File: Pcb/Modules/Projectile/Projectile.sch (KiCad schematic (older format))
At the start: 34 parts, among them J1 JACK_RJ45, Q1 Q_NMOS_GSD, U1 OPA320, U2 OPA320, X1 HOLE, X2 HOLE, X3 HOLE, X4 HOLE

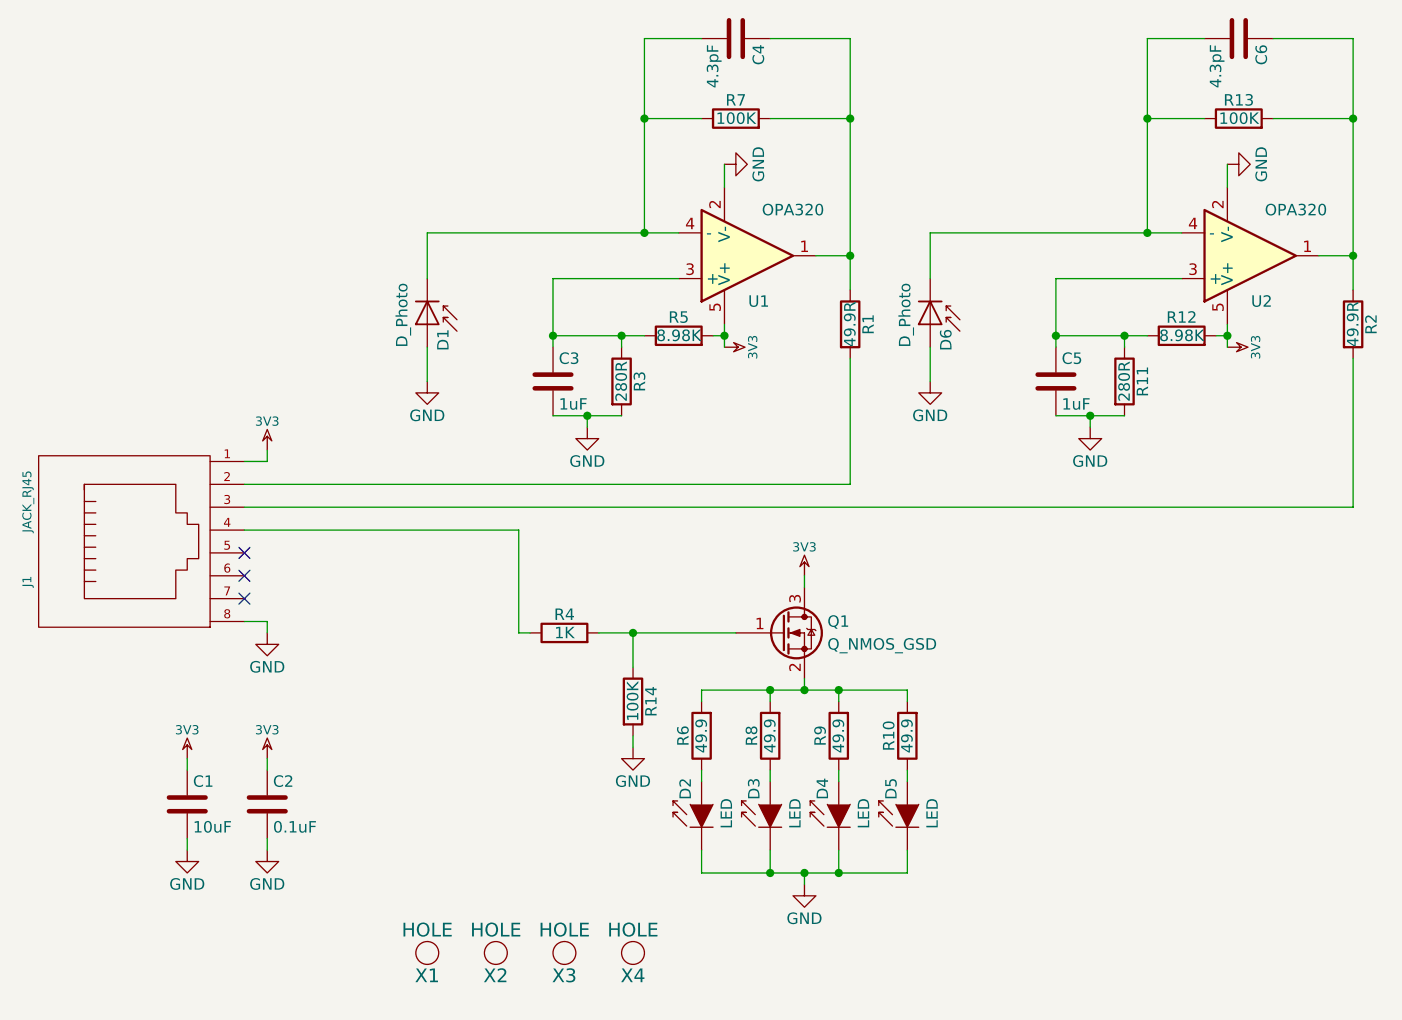
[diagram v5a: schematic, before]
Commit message: Update PCBs to use n channel mosfet on low side
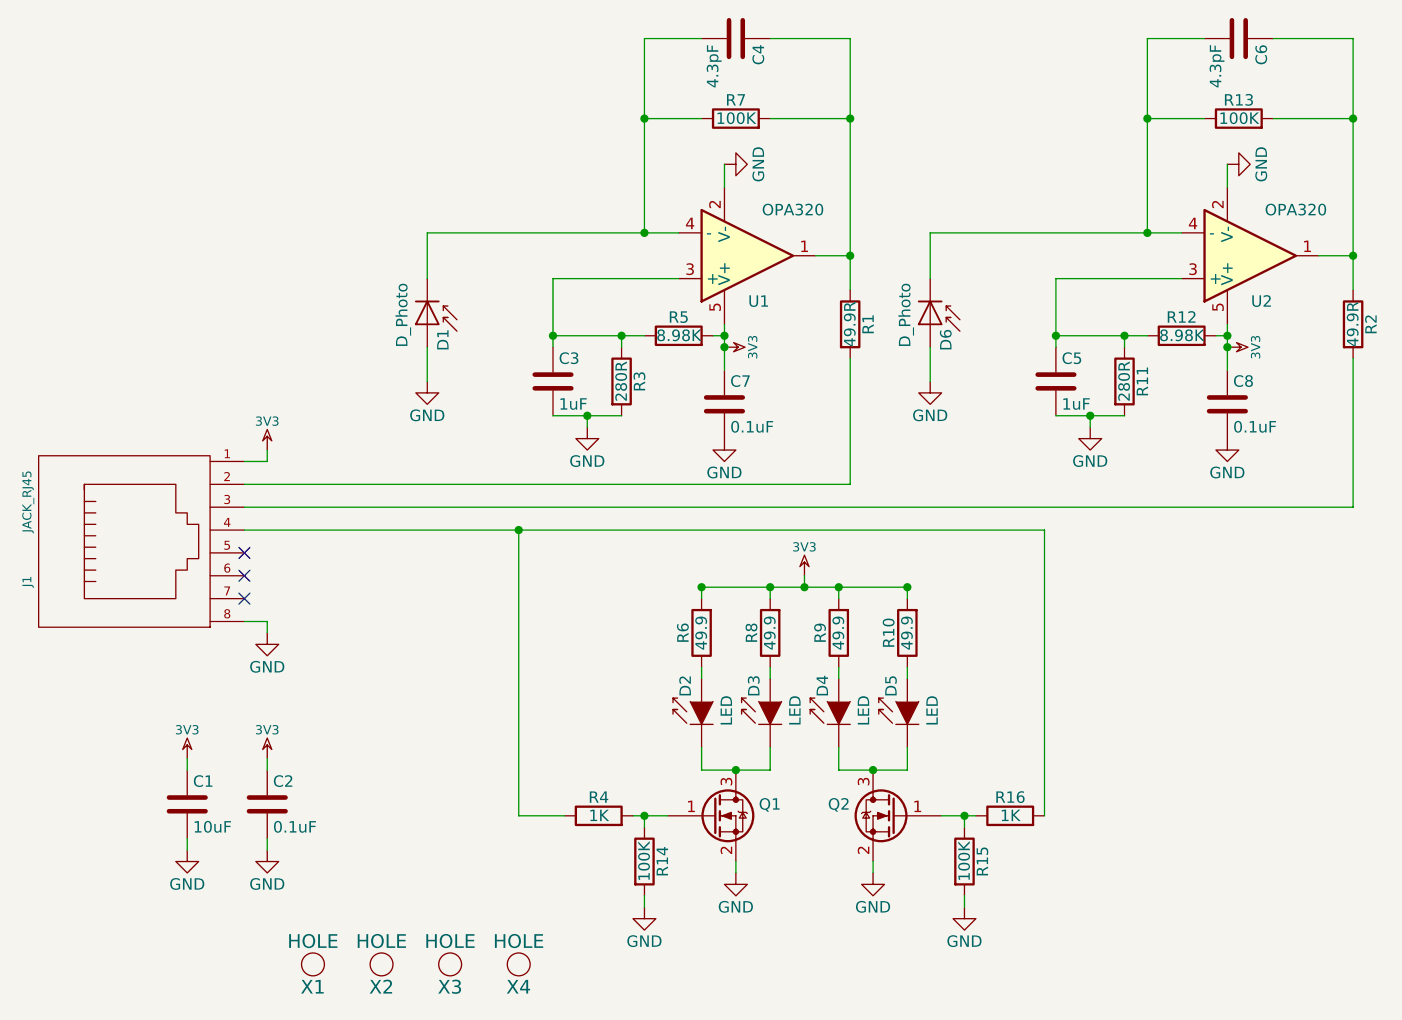
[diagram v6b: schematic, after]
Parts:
- added C7, C8: 0.1uF, Capacitors_SMD:C_0603, symbol C
- added Q2: Q_NMOS_GSD, TO_SOT_Packages_SMD:SOT-23, symbol Q_NMOS_GSD
- added R15: 100K, Resistors_SMD:R_0603, symbol R
- added R16: 1K, Resistors_SMD:R_0603, symbol R
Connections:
- net 3V3: now also R10.2, R6.2, R8.2, R9.2, C7.1, C8.1; no longer Q1.3 (D)
- net GND: now also Q1.2 (S), C7.2, C8.2, Q2.2 (S), R15.2; no longer D2.1 (K), D3.1 (K), D4.1 (K), D5.1 (K)
- net at J1.4, R4.1: now also R16.2
- new net: D2.1 (K), D3.1 (K), Q1.3 (D)
- new net: D4.1 (K), D5.1 (K), Q2.3 (D)
- new net: Q2.1 (G), R15.1, R16.1
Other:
- moved on the sheet: D2, D3, D4, D5, Q1, R10, R14, R4, R6, R8, R9, X1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

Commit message: Change 100K to 10K resistors
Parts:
- R14, R15: value 100K -> 10K
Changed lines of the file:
@@
 P 4400 5550
 F 0 "R14" V 4480 5550 50  0000 C CNN
-F 1 "100K" V 4400 5550 50  0000 C CNN
+F 1 "10K" V 4400 5550 50  0000 C CNN
 F 2 "Resistors_SMD:R_0603" V 4330 5550 50  0001 C CNN
 F 3 "" H 4400 5550 50  0001 C CNN
@@
 P 5800 5550
 F 0 "R15" V 5880 5550 50  0000 C CNN
-F 1 "100K" V 5800 5550 50  0000 C CNN
+F 1 "10K" V 5800 5550 50  0000 C CNN
 F 2 "Resistors_SMD:R_0603" V 5730 5550 50  0001 C CNN
 F 3 "" H 5800 5550 50  0001 C CNN

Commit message: Update pcb for new switch
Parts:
- C1, C2, C3, C4, C5, C6, C7, C8: symbol C -> Device:C
- D1, D6: symbol D_Photo -> Device:D_Photo
- D2, D3, D4, D5: symbol LD274 -> opto:LD274
- J1: symbol JACK_RJ45 -> CA6:JACK_RJ45
- Q1, Q2: symbol Q_NMOS_GSD -> Device:Q_NMOS_GSD
- R1, R10, R11, R12, R13, R14, R15, R16, R2, R3, R4, R5, R6, R7, R8, R9: symbol R -> Device:R
- U1, U2: symbol MCP601 -> Projectile-rescue:MCP601
- X1, X2, X3, X4: symbol HOLE -> CA6:HOLE
